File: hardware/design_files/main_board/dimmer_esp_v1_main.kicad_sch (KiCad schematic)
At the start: 54 parts, among them IC1 PEC11S-929K-S0015, J1 Screw_Terminal_01x03, J2 SM05B-SRSS-TB_LF__SN_, J3 Conn_01x02, K1 FTR-LYCA005Y, Q1 BC817, SW1 Commission, SW2 Toggle, SW3 Reset, U1 SGM2212-3.3XKC3G/TR, U2 USB TYPE-C 16PLT-H10.0, U3 SN74LV1T125DBVR, U4 ESP32-C6-MINI

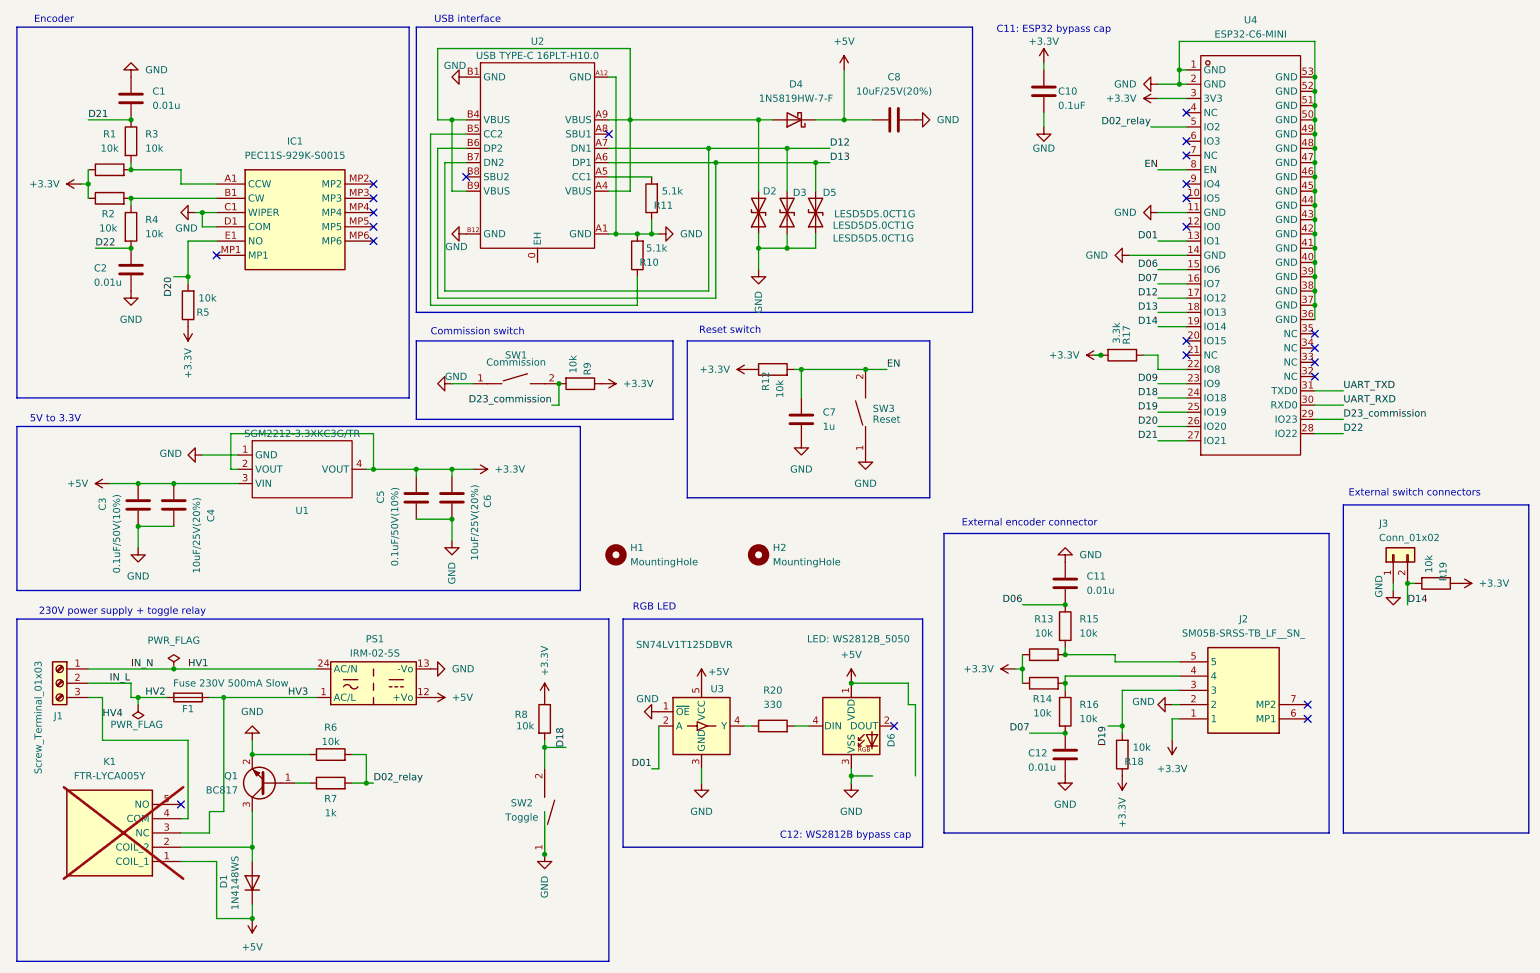
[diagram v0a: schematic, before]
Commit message: Hardware: Smaller fixes
* Missing power flags
* Add missing bypass cap for LED
* Fix labels
* Add test points for GPIO9, TX, RX, and ground
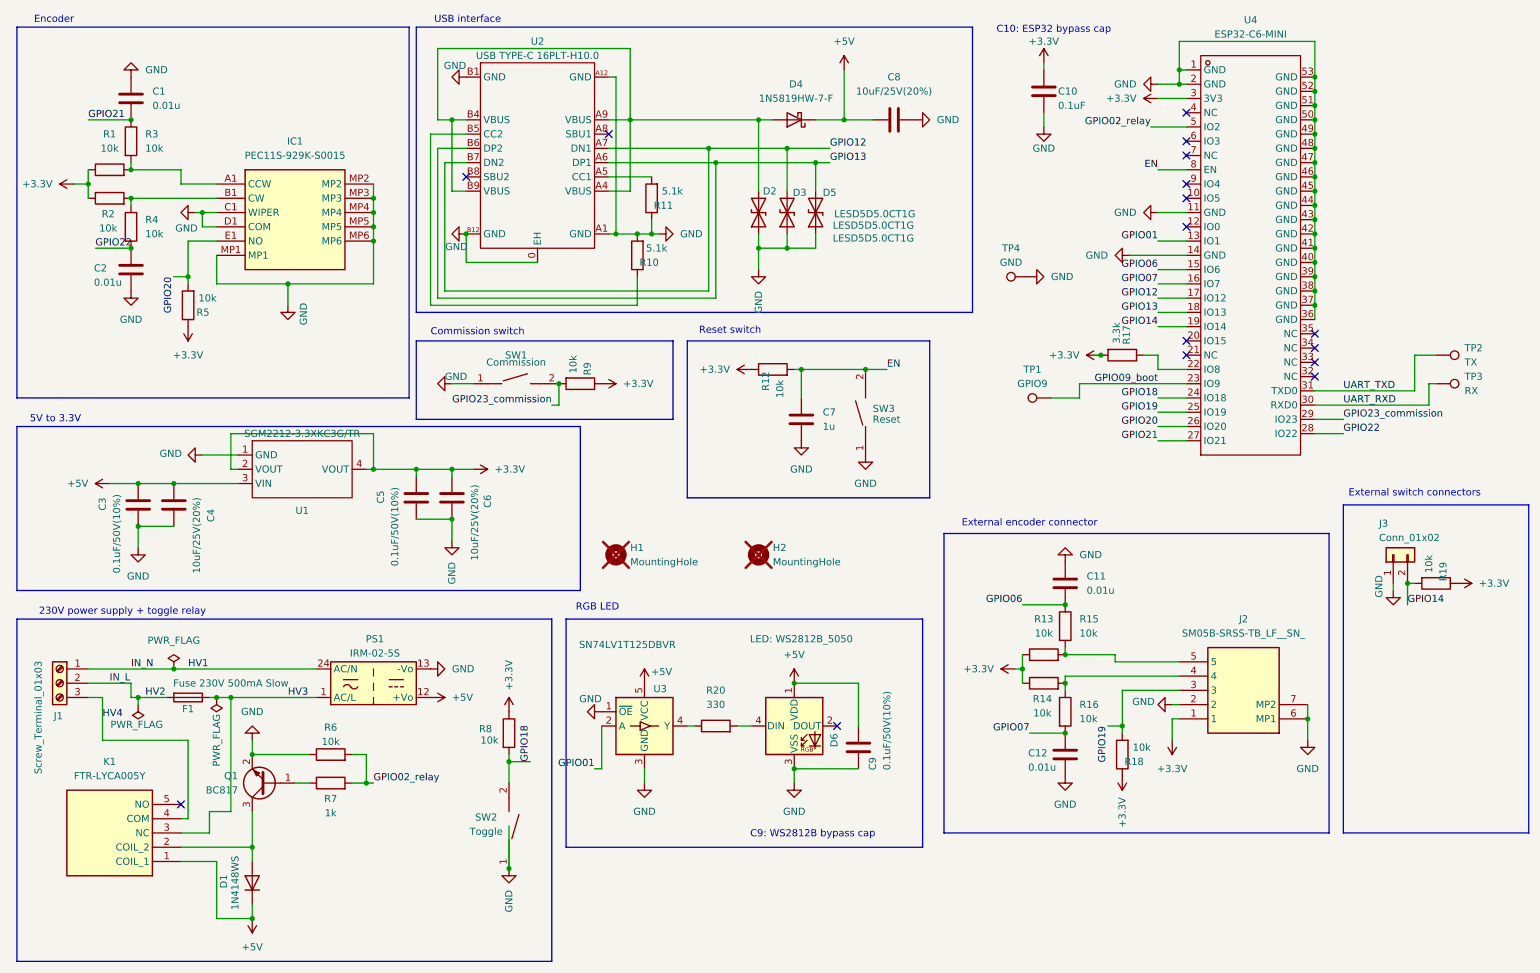
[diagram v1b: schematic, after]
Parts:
- added C9: 0.1uF/50V(10%), Capacitor_SMD:C_0603_1608Metric, symbol Device:C
- added TP1: GPIO9, TestPoint:TestPoint_Pad_D1.5mm, symbol Connector:TestPoint
- added TP2: TX, TestPoint:TestPoint_Pad_D1.5mm, symbol Connector:TestPoint
- added TP3: RX, TestPoint:TestPoint_Pad_D1.5mm, symbol Connector:TestPoint
- added TP4: GND, TestPoint:TestPoint_Pad_D1.5mm, symbol Connector:TestPoint
- H1, H2: now not fitted
- K1: LCSC (none) -> C1222376; now fitted
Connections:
- net +5V: now also C9.1
- net GND: now also IC1.MP1, IC1.MP2, IC1.MP3, IC1.MP4, IC1.MP5, IC1.MP6, J2.6 (MP1), J2.7 (MP2), U2.0 (EH), C9.2, TP4.1
- net UART_RXD: now also TP3.1
- net UART_TXD: now also TP2.1
- net D01 renamed GPIO01
- net D02_relay renamed GPIO02_relay
- net D06 renamed GPIO06
- net D07 renamed GPIO07
- net D09 renamed GPIO09_boot
- net GPIO09_boot: now also TP1.1
- net D12 renamed GPIO12
- net D13 renamed GPIO13
- net D14 renamed GPIO14
- net D18 renamed GPIO18
- net D19 renamed GPIO19
- net D20 renamed GPIO20
- net D21 renamed GPIO21
- net D22 renamed GPIO22
- net D23_commission renamed GPIO23_commission
- no-connect marks 24 -> 16
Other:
- note added: "C10: ESP32 bypass cap"
- note added: "C9: WS2812B bypass cap"
- note removed: "C11: ESP32 bypass cap"
- note removed: "C12: WS2812B bypass cap"
- title: (none) -> Dimmer ESP v1 main
- moved on the sheet: D6, R20, R8, SW2, U3
